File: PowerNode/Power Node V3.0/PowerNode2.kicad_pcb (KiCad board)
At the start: 2 copper layers, 68.6 x 64.1 mm, 54 parts, among them IC1 ACS712xLCTR-30A, IC2 74HC594N, IC3 CD4511B, IC4 CD4511B

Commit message: PN3: more routing changes
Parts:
- R9, U$1: moved to B.Cu
- moved GND2 141.9 mm to (121.9, 133.3)
- moved R7 102.8 mm to (153.0, 105.4)
- moved DP1 98.1 mm to (184.2, 133.3)
- moved IC2 72.0 mm to (115.6, 37.5)
- moved R9 69.7 mm to (180.3, 133.3), turned to -90 degrees
- moved C6 67.8 mm to (145.5, 97.1)
- moved INOUT1 65.9 mm to (153.0, 90.8)
- moved U$1 33.3 mm to (158.1, 116.8)
- moved GNDHIIN1 10.2 mm to (182.9, 95.9)
- moved IC1 10.2 mm to (168.9, 95.9)
- moved R1 10.2 mm to (172.7, 97.8)
- moved R2 10.2 mm to (182.9, 104.8)
- moved S1 10.2 mm to (175.9, 97.8)
- moved C2 10.2 mm to (169.5, 105.4)
- moved GNDHIOUT1 10.2 mm to (167.6, 87.6)
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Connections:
- U$1 pad 10: /IMEAS -> /VMEAS_1
- U$1 pad 8: /VMEAS_1 -> /IMEAS
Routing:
- net Vdd: track 17.9 -> 64.7 mm
- net /VPASS: track 5.65 -> 37.6 mm
- net /SDA: track 0.00 -> 25.8 mm
- net /DP1: track 0.00 -> 19.5 mm
- net /SCL: track 0.00 -> 18.4 mm
- net Vss: track 16.9 -> 27.5 mm
- net /IMEAS: track 0.00 -> 4.66 mm
- net Net-(DP1-Pad1): track 0.00 -> 4.43 mm
- net /VMEAS_1: track 2.94 -> 7.27 mm
- net /VPOT: track 0.00 -> 3.07 mm
- added copper zone on F.Cu, net Vdd
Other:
- board size 68.6 x 64.1 mm -> 68.6 x 54 mm

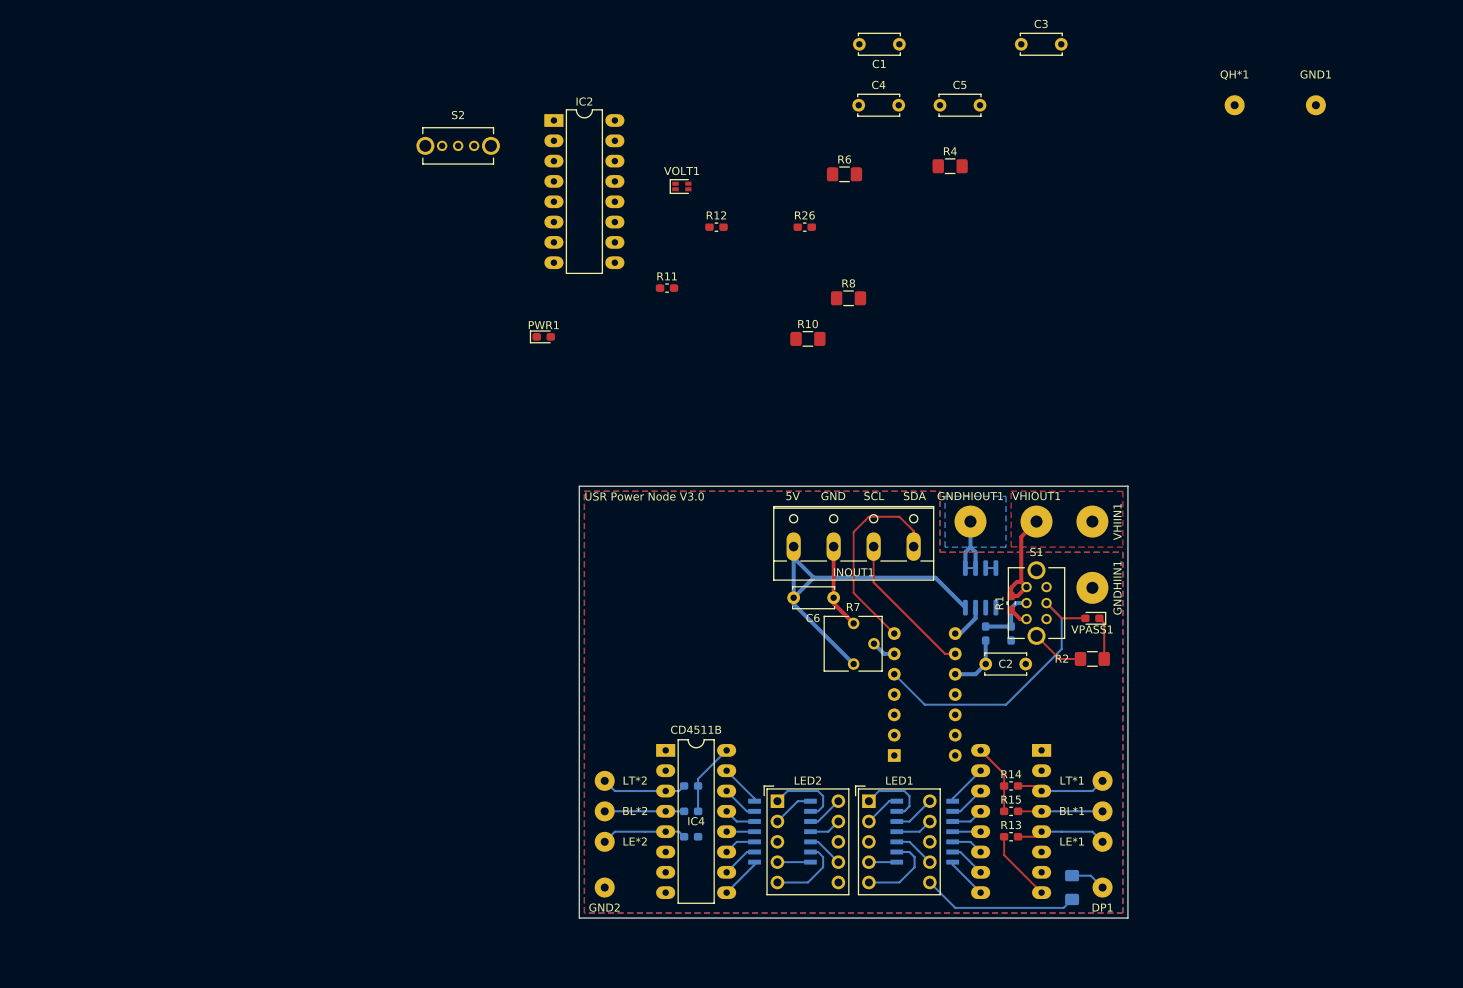
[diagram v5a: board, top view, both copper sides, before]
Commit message: PN3: finished routing
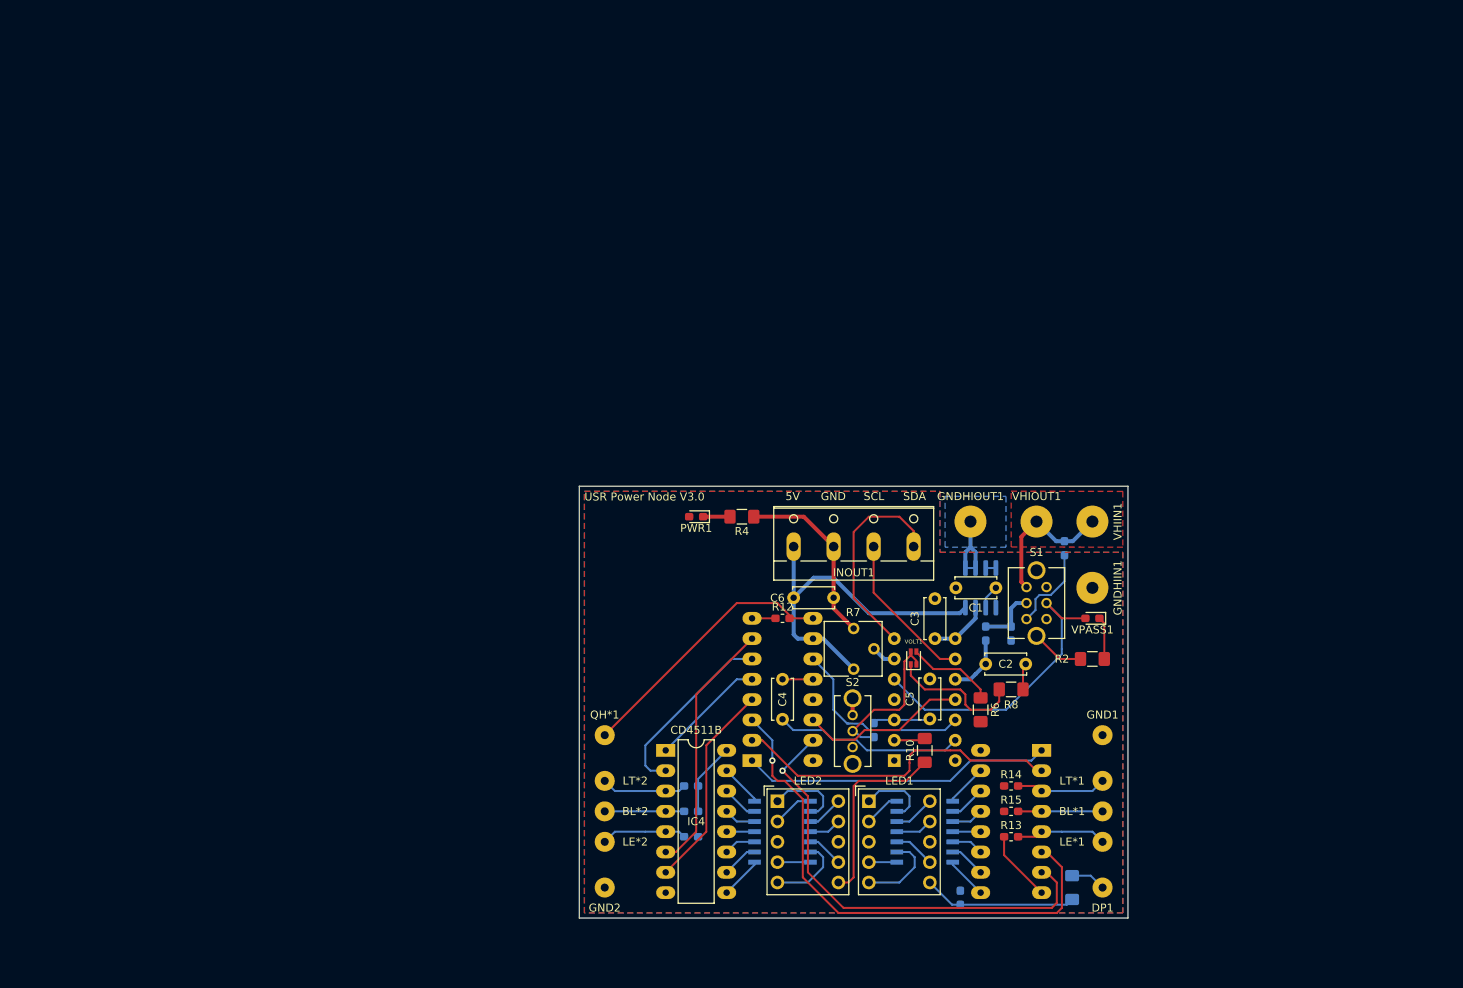
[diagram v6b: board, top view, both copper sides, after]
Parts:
- IC2, R1, R11, R26: moved to B.Cu
- moved QH*1 111.4 mm to (121.9, 114.3)
- moved S2 88.2 mm to (152.9, 113.8), turned to 90 degrees
- moved R26 86.0 mm to (166.4, 134.6), turned to -90 degrees
- moved IC2 83.8 mm to (140.3, 117.5)
- moved GND1 83.1 mm to (184.2, 114.3)
- moved C5 76.7 mm to (162.6, 112.3), turned to 90 degrees
- moved C3 75.1 mm to (163.2, 102.2), turned to 90 degrees
- moved C4 72.4 mm to (144.1, 107.3), turned to -90 degrees
- moved R6 69.1 mm to (168.9, 111.1), turned to -90 degrees
- moved C1 69.0 mm to (170.8, 95.9)
- moved VOLT1 65.7 mm to (160.5, 104.6), turned to 90 degrees
- moved R11 61.0 mm to (155.6, 113.7), turned to -90 degrees
- moved R10 53.5 mm to (161.9, 116.2), turned to 90 degrees
- moved R8 52.9 mm to (172.7, 108.6), turned to 180 degrees
- moved R4 51.0 mm to (139.1, 87.0), turned to 180 degrees
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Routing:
- net Net-(IC2-Pad3): track 0.00 -> 65.7 mm, vias 0 -> 1
- net Net-(IC2-Pad15): track 0.00 -> 57.6 mm, vias 0 -> 1
- net Net-(IC2-Pad2): track 0.00 -> 41.5 mm
- net Net-(IC2-Pad1): track 0.00 -> 38.8 mm
- net /nQH: track 0.00 -> 33.9 mm
- net Net-(IC2-Pad7): track 0.00 -> 31.9 mm
- net Net-(IC2-Pad4): track 0.00 -> 26.1 mm
- net Net-(IC2-Pad11): track 0.00 -> 24.2 mm
- net Net-(C4-Pad2): track 0.00 -> 23.7 mm
- net /DP2: track 0.00 -> 23.7 mm
- net Net-(IC2-Pad6): track 0.00 -> 23.1 mm
- net Net-(IC2-Pad14): track 0.00 -> 20.9 mm
- net Vss: track 27.5 -> 48.0 mm
- net /SWITCH: track 0.00 -> 19.7 mm
- net Net-(R8-Pad2): track 0.00 -> 16.9 mm
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
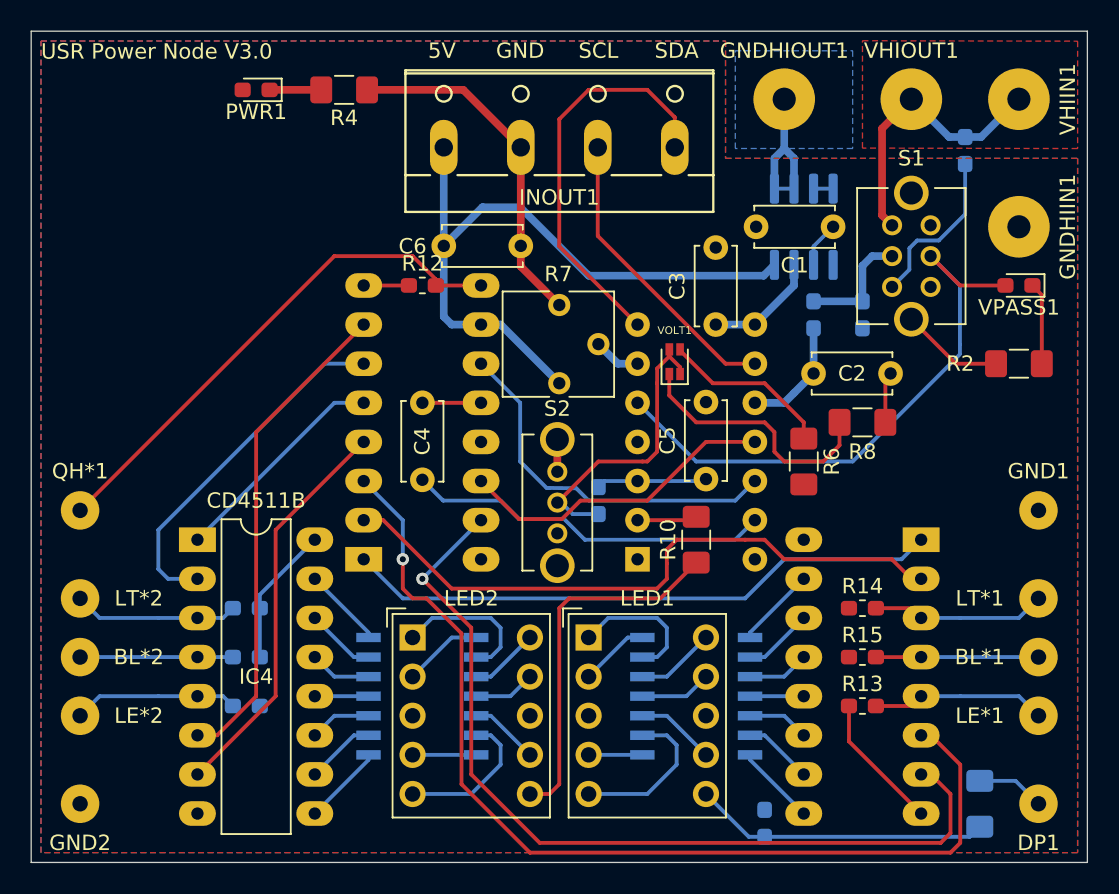
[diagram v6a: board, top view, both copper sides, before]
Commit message: PN3: added logos and cleaned up connections
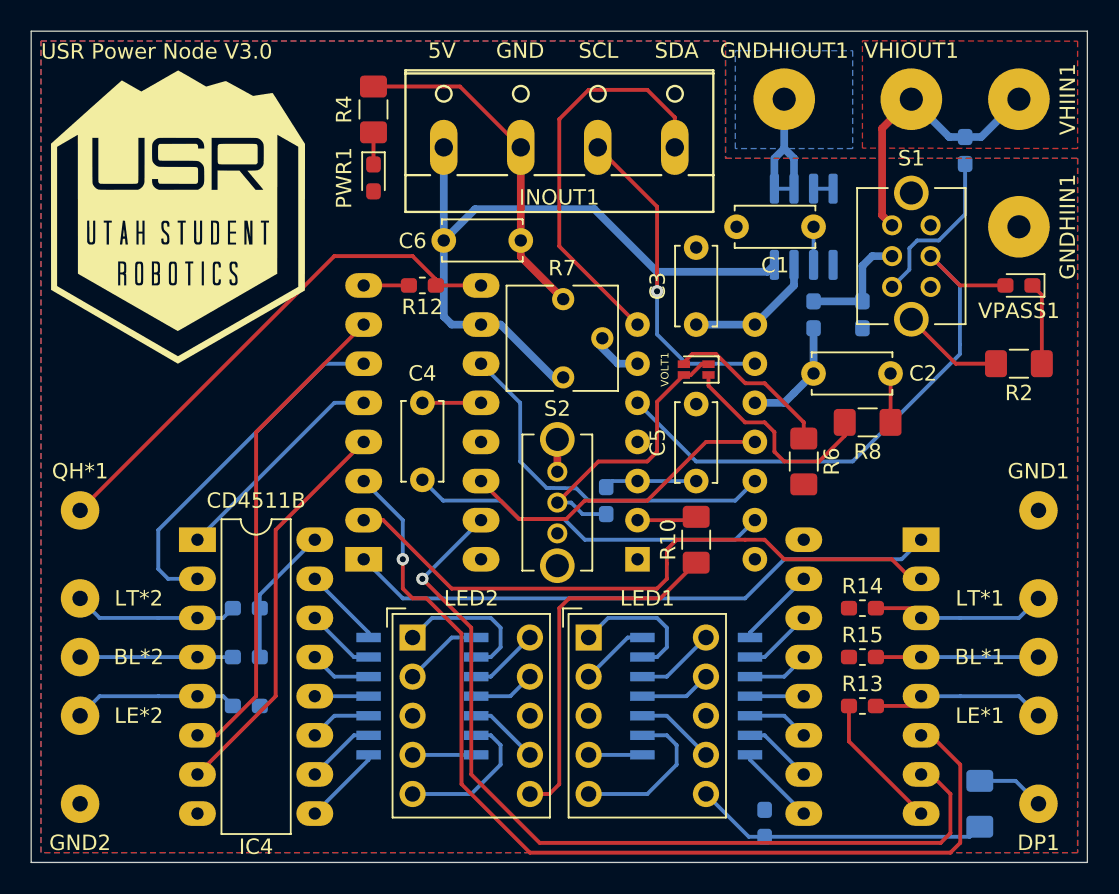
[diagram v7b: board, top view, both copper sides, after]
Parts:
- added G***: LOGO, PowerNode2:USR, F.Cu at (128.3, 95.2)
- moved PWR1 9.52 mm to (141.0, 92.7), turned to -90 degrees
- moved R4 2.29 mm to (141.0, 88.3), turned to -90 degrees
- moved VOLT1 1.49 mm to (161.9, 105.2), turned to 180 degrees
- moved C1 1.27 mm to (169.5, 95.9)
- moved C3 1.27 mm to (161.9, 102.2)
- moved C5 0.65 mm to (161.9, 112.4)
- moved R11 0.51 mm to (156.1, 113.7)
- moved R7 0.46 mm to (153.3, 105.7)
- moved C6 0.35 mm to (145.5, 96.8)
- moved R8 0.34 mm to (173.1, 108.6)
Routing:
- net Net-(R8-Pad2): track 16.9 -> 13.9 mm
- net /SCL: track 20.0 -> 21.5 mm, vias 0 -> 1
- net Net-(PWR1-Pad1): track 3.35 -> 2.08 mm
- net /IMEAS: track 7.47 -> 8.74 mm
- net Net-(C5-Pad1): track 7.20 -> 6.19 mm
- net Vss: track 48.0 -> 47.3 mm
- net Net-(C1-Pad1): track 3.00 -> 2.47 mm
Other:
- board text added: "Designed by Alex Charters and Jonathan Warner github.com/utahrobotics/Electrical-2019-2020"

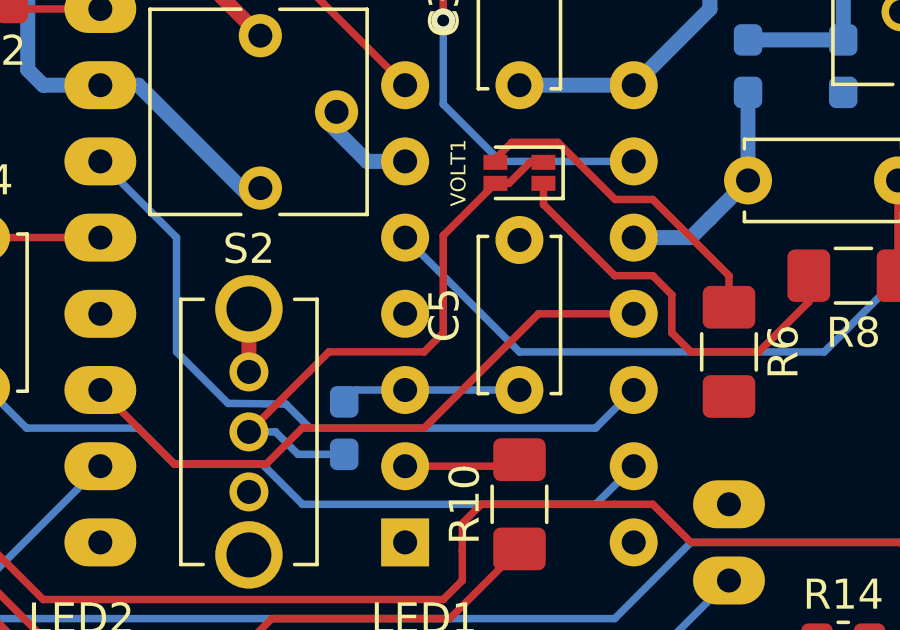
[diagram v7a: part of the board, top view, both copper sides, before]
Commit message: PN3: created 3D models and small board changes
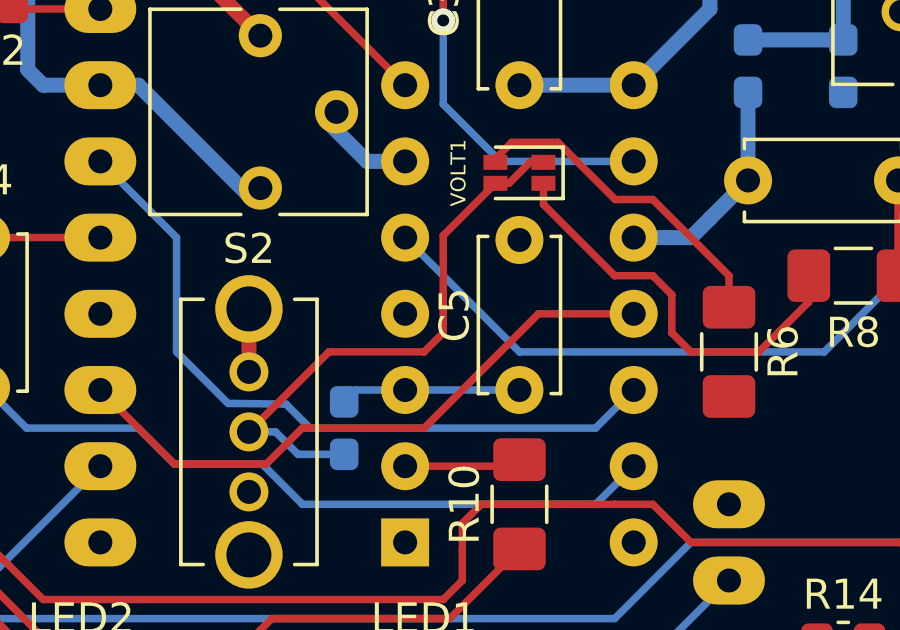
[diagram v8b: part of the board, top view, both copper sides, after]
